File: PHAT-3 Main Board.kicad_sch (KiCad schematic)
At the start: 17 parts, among them K1 G5LE-1, P1 Power Terminal Block, P2 Power Terminal Block, P3 Power Terminal Block, P4 Power Terminal Block, U1 AHT21, U10 Logic Level Converter, U2 ESP32-S3 Dual-core SX1262, U3 BME280, U4 GY-521 MPU-6050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

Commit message: First Wiring Draft
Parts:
- removed K1: G5LE-1, Relay_THT:Relay_SPDT_Omron-G5LE-1, symbol Relay:G5LE-1
- added Q1: IRLZ44N, Package_TO_SOT_THT:TO-220-3_Vertical, symbol Transistor_FET:IRLZ44N
- added R3: 10k, Resistor_THT:R_Axial_DIN0207_L6.3mm_D2.5mm_P10.16mm_Horizontal, symbol Device:R
- R1, R2: value R -> 10k
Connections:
- net GND: now also P2.1 (GND), P4.1 (GND), U9.6 (GND), Q1.3 (S), R3.1; no longer U7.1 (GND)
- net at U6.2 (TXD): now also U2.10 (U2RXD); no longer U2.36 (U1RTS)
- net at U6.3 (RXD): now also U2.9 (U2TXD); no longer U2.35 (U1CTS)
- net +5V: now reaches U1.1 (VIN), U10.10 (HV), U2.20 (5V), U3.1 (VIN), U4.1 (VCC), U5.2 (OUT+), U6.5 (VCC), U7.2 (VDD), U8.1 (5V)
- net +5V: now also P2.2 (PWR), P4.2 (PWR), R1.1, R2.2, U9.5 (VCC)
- net at R2.1: now also U1.3 (SCL), U10.11 (HV2), U3.3 (SCL), U4.3 (SCL), U7.3 (SCL)
- net at U1.4 (SDA), U3.4 (SDA), U4.4 (SDA)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: now also R1.2, U10.12 (HV1); no longer U10.11 (HV2)
- net at U9.1 (CS): now also U2.29 (CS)
- net at U9.2 (SCK): now also U2.30 (SCK)
- net at U9.3 (MOSI): now also U2.31 (MOSI)
- net at U9.4 (MISO): now also U2.32 (MISO), R3.2
- net +15V: now reaches P1.2 (PWR), U5.1 (IN+)
- net +15V: now also P3.2 (PWR)
- net at U2.11 (U1TXD): now also U8.3 (RX)
- net at U2.12 (U1RXD): now also U8.2 (TX)
- net at U2.13 (SCL): now also U10.2 (LV2)
- net at U2.14 (SDA): now also U10.1 (LV1)
- net at U2.16 (3V3): now also U10.3 (LV)
- net at U2.22 (Ve): no longer U10.3 (LV)
- net at U2.23 (U0RXD): no longer U8.2 (TX)
- net at U2.24 (U0TXD): no longer U8.3 (RX)
- net at U2.27 (DATA): no longer U10.2 (LV2)
- net at U2.28 (HTR): now also Q1.1 (G); no longer U10.1 (LV1)
- net at P3.1 (GND): now also Q1.2 (D)
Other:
- note added: "Heater switch"
- note added: "Thumbcam power terminals"
- moved on the sheet: P1, P2, P3, P4, R1, R2, U1, U10, U2, U3, U4, U5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

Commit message: Finished Wiring and Implemented MOSFET
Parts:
- added R4: 100, Resistor_THT:R_Axial_DIN0207_L6.3mm_D2.5mm_P10.16mm_Horizontal, symbol Device:R
- added R5: 10k, Resistor_THT:R_Axial_DIN0207_L6.3mm_D2.5mm_P10.16mm_Horizontal, symbol Device:R
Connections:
- net GND: now also U2.18 (GND), U7.1 (GND), R5.1
- net at Q1.1 (G): now also R4.2, R5.2; no longer U2.28 (HTR)
- new net: R4.1, U2.28 (HTR)
- no-connect marks 0 -> 31
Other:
- moved on the sheet: P3, Q1, R3, U2, U9

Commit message: Rewired Everything Again
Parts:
- removed U3: BME280, Actual Footprint Library:BME280, symbol Footprint Library:BME280
- added C1: 100uF, Capacitor_THT:C_Radial_D5.0mm_H11.0mm_P2.00mm, symbol Device:C
- added C2, C3: 100nF, Capacitor_THT:C_Disc_D3.0mm_W2.0mm_P2.50mm, symbol Device:C
- added R6, R7: 10k, Resistor_THT:R_Axial_DIN0207_L6.3mm_D2.5mm_P10.16mm_Horizontal, symbol Device:R
- added U3: GY-68 BMP180, Actual Footprint Library:GY-68 BMP180, symbol Footprint Library:GY-68 BMP180
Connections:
- net +5V: now also C1.1, C2.2; no longer U1.1 (VIN), U7.2 (VDD)
- net GND: now also C1.2, C2.1, C3.2, U3.2 (GND)
- net at U2.13 (SCL): now also U1.3 (SCL), U10.1 (LV1), U7.3 (SCL), R7.2, U3.3 (SCL); no longer U10.2 (LV2)
- net at U2.14 (SDA): now also U1.4 (SDA), U10.2 (LV2), U7.4 (SDA), R6.2, U3.4 (SDA); no longer U10.1 (LV1)
- net at U2.16 (3V3): no longer U10.3 (LV)
- net +3V3: now reaches U2.17 (3V3)
- net +3V3: now also U1.1 (VIN), U10.3 (LV), U7.2 (VDD), C3.1, R6.1, R7.1, U3.1 (VIN)
- new net: R2.1, U10.11 (HV2), U4.4 (SDA)
- new net: R1.2, U10.12 (HV1), U4.3 (SCL)
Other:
- note added: "Buck converter"
- moved on the sheet: P1, P2, P3, P4, Q1, R1, R2, R3, R4, R5, U10, U2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

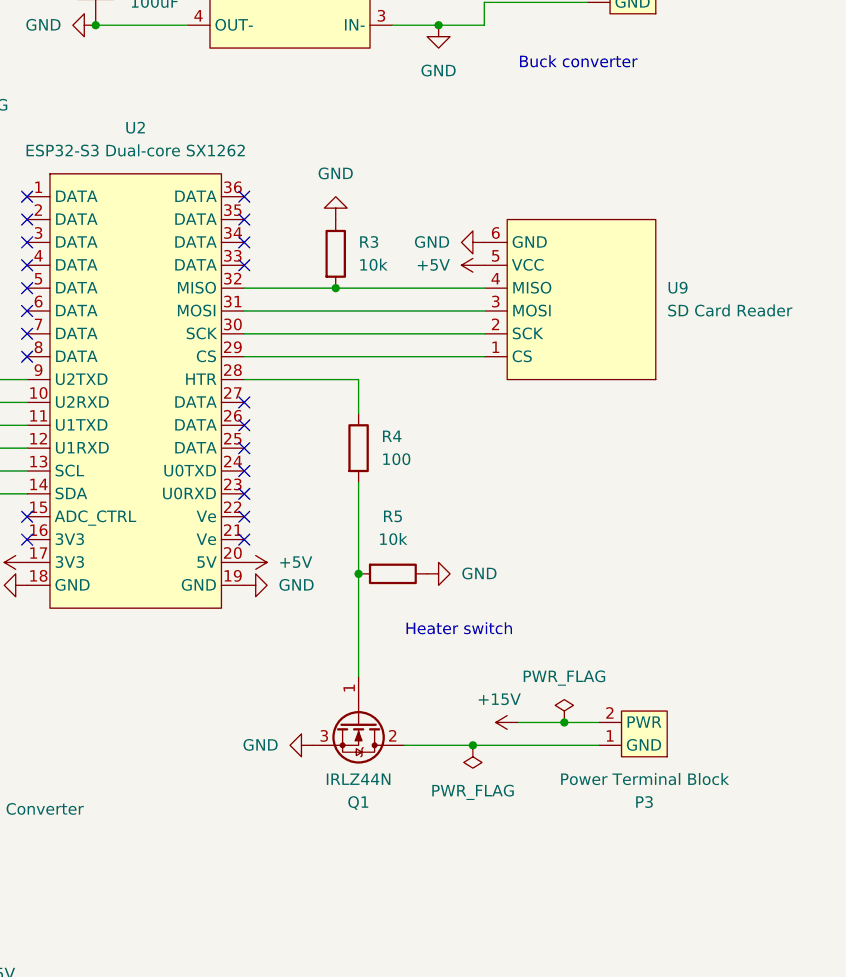
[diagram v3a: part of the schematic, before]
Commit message: Updated Footprint Sizes and SD Card Reader
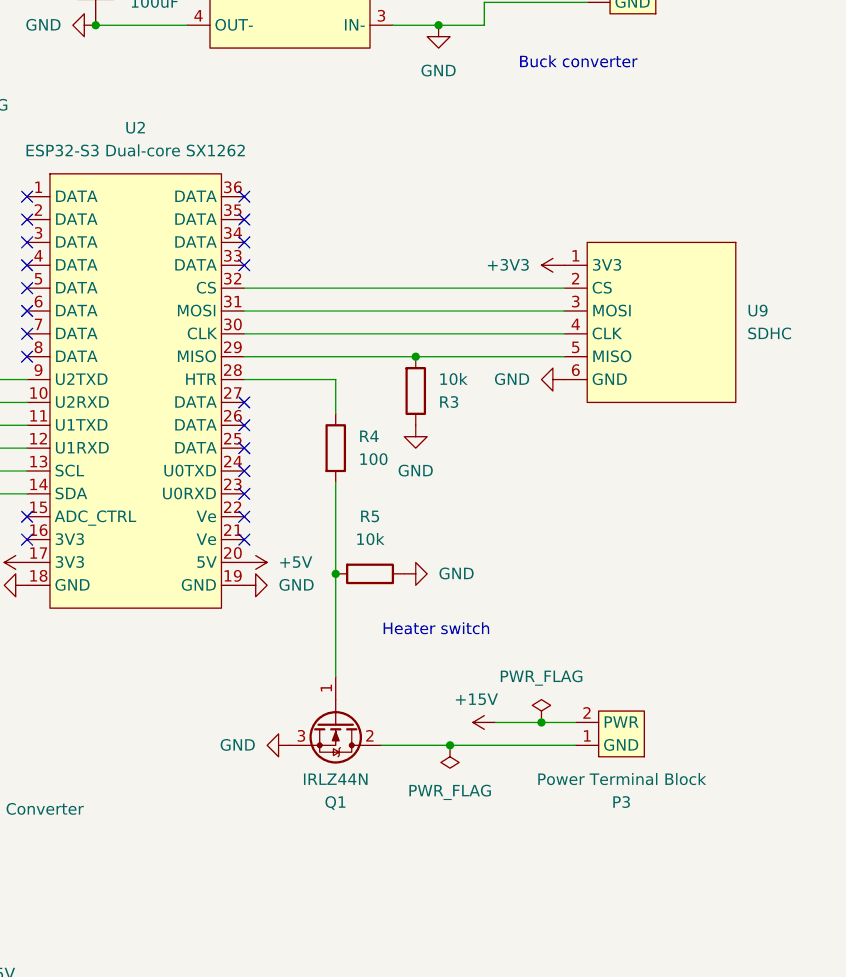
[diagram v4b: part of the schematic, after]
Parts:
- removed U9: SD Card Reader, Actual Footprint Library:SD Card Reader, symbol Footprint Library:SD_Card_Reader
- added U9: SDHC, Actual Footprint Library:SDHC, symbol Footprint Library:SDHC
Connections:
- net +3V3: now also U9.1 (3V3)
- net GND: now also U9.6 (GND)
- net at U2.29 (MISO): now also R3.2, U9.5 (MISO)
- net at U2.30 (CLK): now also U9.4 (CLK)
- net at U2.31 (MOSI): now also U9.3 (MOSI)
- net at U2.32 (CS): now also U9.2 (CS); no longer R3.2
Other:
- moved on the sheet: P3, Q1, R3, R4, R5

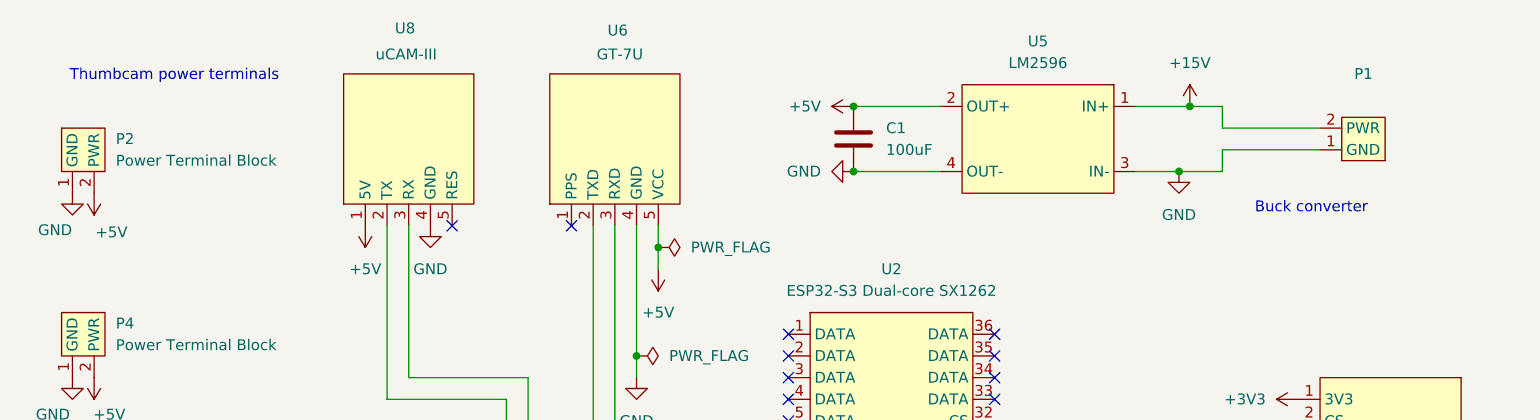
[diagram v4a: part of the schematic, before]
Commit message: Made a Preliminary PCB Layout
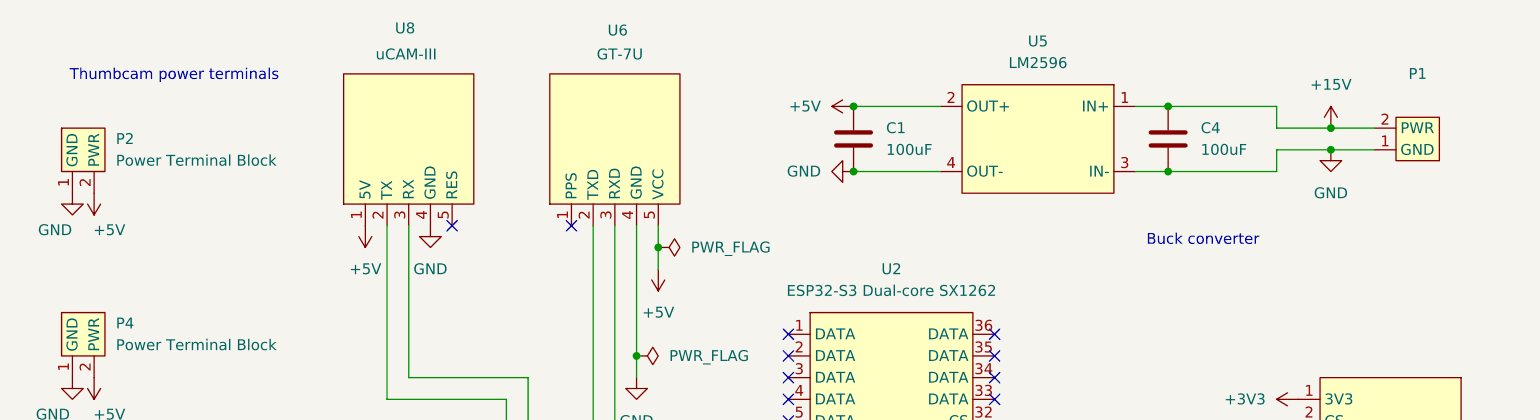
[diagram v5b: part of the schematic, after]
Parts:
- added C4: 100uF, Capacitor_THT:C_Radial_D5.0mm_H11.0mm_P2.00mm, symbol Device:C
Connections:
- net +15V: now also C4.1
- net GND: now also C4.2
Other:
- moved on the sheet: P1
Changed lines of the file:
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@@
 	)
 	(junction
+		(at 215.9 41.91)
+		(diameter 0)
+		(color 0 0 0 0)
+	)
+	(junction
 		(at 186.69 107.95)
 		(diameter 0)
@@
 	)
 	(junction
-		(at 199.39 39.37)
+		(at 95.25 121.92)
 		(diameter 0)
 		(color 0 0 0 0)
 	)
 	(junction
-		(at 95.25 121.92)
+		(at 196.85 46.99)
 		(diameter 0)
 		(color 0 0 0 0)
@@
 	)
 	(junction
+		(at 215.9 44.45)
+		(diameter 0)
+		(color 0 0 0 0)
+	)
+	(junction
 		(at 133.35 99.06)
 		(diameter 0)
@@
 	)
 	(junction
-		(at 198.12 46.99)
+		(at 95.25 96.52)
 		(diameter 0)
 		(color 0 0 0 0)
 	)
 	(junction
-		(at 95.25 96.52)
+		(at 209.55 124.46)
 		(diameter 0)
 		(color 0 0 0 0)
 	)
 	(junction
-		(at 209.55 124.46)
+		(at 133.35 157.48)
 		(diameter 0)
 		(color 0 0 0 0)
 	)
 	(junction
-		(at 133.35 157.48)
+		(at 196.85 39.37)
 		(diameter 0)
 		(color 0 0 0 0)
@@
 	(wire
 		(pts
+			(xy 196.85 39.37) (xy 209.55 39.37)
+		)
+		(stroke
+			(width 0)
+			(type default)
+		)
+	)
+	(wire
+		(pts
 			(xy 119.38 111.76) (xy 128.27 111.76)
 		)
@@
 	(wire
 		(pts
+			(xy 215.9 41.91) (xy 209.55 41.91)
+		)
+		(stroke
+			(width 0)
+			(type default)
+		)
+	)
+	(wire
+		(pts
 			(xy 95.25 121.92) (xy 95.25 149.86)
 		)
@@
 	(wire
 		(pts
-			(xy 203.2 44.45) (xy 203.2 46.99)
+			(xy 209.55 44.45) (xy 209.55 46.99)
 		)
 		(stroke
@@
 	(wire
 		(pts
-			(xy 203.2 46.99) (xy 198.12 46.99)
+			(xy 193.04 46.99) (xy 196.85 46.99)
 		)
 		(stroke
@@
 	(wire
 		(pts
+			(xy 215.9 44.45) (xy 209.55 44.45)
+		)
+		(stroke
+			(width 0)
+			(type default)
+		)
+	)
+	(wire
+		(pts
 			(xy 160.02 46.99) (xy 170.18 46.99)
 		)
@@
 	(wire
 		(pts
-			(xy 203.2 39.37) (xy 199.39 39.37)
+			(xy 193.04 39.37) (xy 196.85 39.37)
 		)
 		(stroke
@@
 	(wire
 		(pts
-			(xy 203.2 41.91) (xy 203.2 39.37)
+			(xy 209.55 41.91) (xy 209.55 39.37)
 		)
 		(stroke
@@
 	(wire
 		(pts
-			(xy 214.63 44.45) (xy 203.2 44.45)
+			(xy 220.98 44.45) (xy 215.9 44.45)
 		)
 		(stroke
@@
 	(wire
 		(pts
-			(xy 198.12 46.99) (xy 193.04 46.99)
+			(xy 92.71 119.38) (xy 92.71 147.32)
 		)
 		(stroke
@@
 	(wire
 		(pts
-			(xy 92.71 119.38) (xy 92.71 147.32)
+			(xy 160.02 39.37) (xy 170.18 39.37)
 		)
 		(stroke
@@
 	(wire
 		(pts
-			(xy 160.02 39.37) (xy 170.18 39.37)
+			(xy 121.92 71.12) (xy 121.92 91.44)
 		)
 		(stroke
@@
 	(wire
 		(pts
-			(xy 121.92 71.12) (xy 121.92 91.44)
+			(xy 119.38 148.59) (xy 130.81 148.59)
 		)
 		(stroke
@@
 	(wire
 		(pts
-			(xy 119.38 148.59) (xy 130.81 148.59)
+			(xy 135.89 138.43) (xy 135.89 152.4)
 		)
 		(stroke
@@
 	(wire
 		(pts
-			(xy 135.89 138.43) (xy 135.89 152.4)
+			(xy 196.85 46.99) (xy 209.55 46.99)
 		)
 		(stroke
@@
 	(wire
 		(pts
-			(xy 214.63 41.91) (xy 203.2 41.91)
+			(xy 220.98 41.91) (xy 215.9 41.91)
 		)
 		(stroke
@@
 	(wire
 		(pts
-			(xy 199.39 39.37) (xy 193.04 39.37)
-		)
-		(stroke
-			(width 0)
-			(type default)
-		)
-	)
-	(wire
-		(pts
 			(xy 186.69 107.95) (xy 186.69 119.38)
 		)
@@
 	(text "Buck converter"
 		(exclude_from_sim no)
-		(at 213.614 51.308 0)
+		(at 200.914 55.118 0)
 		(effects
 			(font
@@
 	(symbol
 		(lib_id "Device:C")
+		(at 196.85 43.18 0)
+		(unit 1)
+		(exclude_from_sim no)
+		(in_bom yes)
+		(on_board yes)
+		(dnp no)
+		(fields_autoplaced yes)
+		(property "Reference" "C4"
+			(at 200.66 41.9099 0)
+			(effects
+				(font
+					(size 1.27 1.27)
+				)
+				(justify left)
+			)
+		)
+		(property "Value" "100uF"
+			(at 200.66 44.4499 0)
+			(effects
+				(font
+					(size 1.27 1.27)
+				)
+				(justify left)
+			)
+		)
+		(property "Footprint" "Capacitor_THT:C_Radial_D5.0mm_H11.0mm_P2.00mm"
+			(at 197.8152 46.99 0)
+			(effects
+				(font
+					(size 1.27 1.27)
+				)
+				(hide yes)
+			)
+		)
+		(property "Datasheet" "~"
+			(at 196.85 43.18 0)
+			(effects
+				(font
+					(size 1.27 1.27)
+				)
+				(hide yes)
+			)
+		)
+		(property "Description" "Unpolarized capacitor"
+			(at 196.85 43.18 0)
+			(effects
+				(font
+					(size 1.27 1.27)
+				)
+				(hide yes)
+			)
+		)
+		(pin "2"
+		)
+		(pin "1"
+		)
+		(instances
+			(project "PHAT-3 Main Board"
+				(path "/da389c8a-9ca2-41c4-a7eb-3ce46ba4333b"
+					(reference "C4")
+					(unit 1)
+				)
+			)
+		)
+	)
+	(symbol
+		(lib_id "Device:C")
 		(at 160.02 43.18 0)
 		(unit 1)
@@
 		)
 		(property "Value" "+5V"
-			(at 73.152 54.102 0)
+			(at 72.898 53.848 0)
 			(effects
 				(font
@@
 	(symbol
 		(lib_id "Footprint Library:Power_Terminal_Block")
-		(at 217.17 44.45 270)
+		(at 223.52 44.45 270)
 		(mirror x)
 		(unit 1)
@@
 		(dnp no)
 		(property "Reference" "P1"
-			(at 219.71 35.56 90)
+			(at 226.06 35.56 90)
 			(effects
 				(font
@@
 		)
 		(property "Value" "Power Terminal Block"
-			(at 219.71 38.1 90)
+			(at 226.06 38.1 90)
 			(effects
 				(font
@@
 		)
 		(property "Footprint" "TerminalBlock_Phoenix:TerminalBlock_Phoenix_MKDS-1,5-2-5.08_1x02_P5.08mm_Horizontal"
-			(at 224.282 44.45 0)
+			(at 230.632 44.45 0)
 			(effects
 				(font
@@
 		)
 		(property "Datasheet" ""
-			(at 217.17 44.45 0)
+			(at 223.52 44.45 0)
 			(effects
 				(font
@@
 		)
 		(property "Description" ""
-			(at 217.17 44.45 0)
+			(at 223.52 44.45 0)
 			(effects
 				(font
@@
 	(symbol
 		(lib_id "power:+15V")
-		(at 199.39 39.37 0)
+		(at 215.9 41.91 0)
 		(unit 1)
 		(exclude_from_sim no)
@@
 		(fields_autoplaced yes)
 		(property "Reference" "#PWR030"
-			(at 199.39 43.18 0)
+			(at 215.9 45.72 0)
 			(effects
 				(font
@@
 		)
 		(property "Value" "+15V"
-			(at 199.39 34.29 0)
+			(at 215.9 36.83 0)
 			(effects
 				(font
@@
 		)
 		(property "Footprint" ""
-			(at 199.39 39.37 0)
+			(at 215.9 41.91 0)
 			(effects
 				(font
@@
 		)
 		(property "Datasheet" ""
-			(at 199.39 39.37 0)
+			(at 215.9 41.91 0)
 			(effects
 				(font
@@
 		)
 		(property "Description" "Power symbol creates a global label with name \"+15V\""
-			(at 199.39 39.37 0)
+			(at 215.9 41.91 0)
 			(effects
 				(font
@@
 	(symbol
 		(lib_id "power:GND")
-		(at 198.12 46.99 0)
+		(at 215.9 44.45 0)
 		(unit 1)
 		(exclude_from_sim no)
@@
 		(fields_autoplaced yes)
 		(property "Reference" "#PWR031"
-			(at 198.12 53.34 0)
+			(at 215.9 50.8 0)
 			(effects
 				(font
@@
 		)
 		(property "Value" "GND"
-			(at 198.12 52.07 0)
+			(at 215.9 49.53 0)
 			(effects
 				(font
@@
 		)
 		(property "Footprint" ""
-			(at 198.12 46.99 0)
+			(at 215.9 44.45 0)
 			(effects
 				(font
@@
 		)
 		(property "Datasheet" ""
-			(at 198.12 46.99 0)
+			(at 215.9 44.45 0)
 			(effects
 				(font
@@
 		)
 		(property "Description" "Power symbol creates a global label with name \"GND\" , ground"
-			(at 198.12 46.99 0)
+			(at 215.9 44.45 0)
 			(effects
 				(font

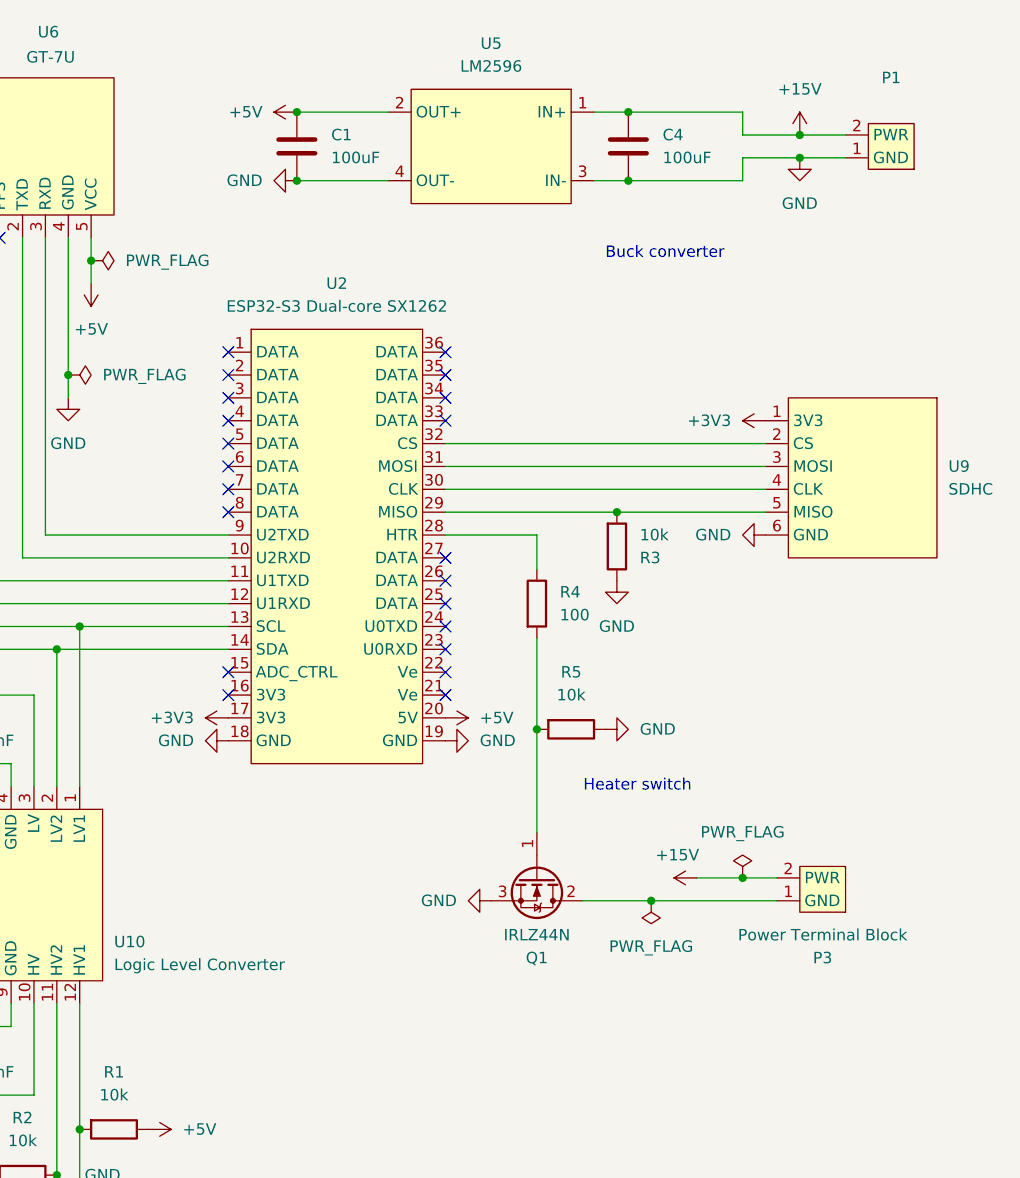
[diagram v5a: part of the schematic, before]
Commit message: Added Diodes and Switch
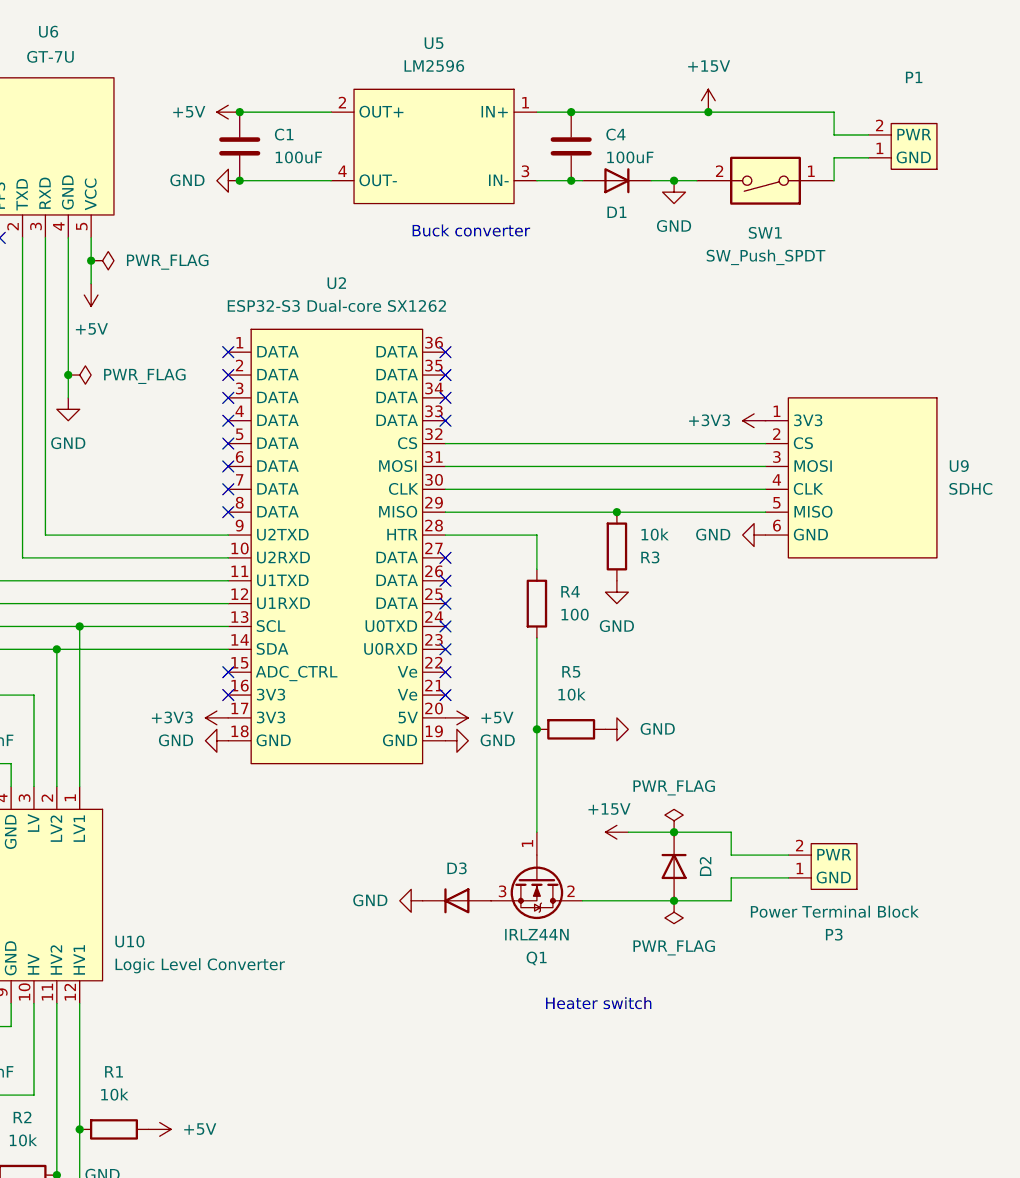
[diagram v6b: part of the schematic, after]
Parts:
- added D1, D2, D3: ~, Diode_THT:D_DO-27_P12.70mm_Horizontal, symbol Device:D
- added SW1: SW_Push_SPDT, Button_Switch_THT:SW_DIP_SPSTx01_Slide_9.78x4.72mm_W7.62mm_P2.54mm, symbol Switch:SW_DIP_x01
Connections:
- net +15V: now also D2.1 (K)
- net GND: now also D1.1 (K), D3.1 (K), SW1.2; no longer C4.2, P1.1 (GND), Q1.3 (S), U5.3 (IN-)
- net at P3.1 (GND), Q1.2 (D): now also D2.2 (A)
- new net: D3.2 (A), Q1.3 (S)
- new net: C4.2, D1.2 (A), U5.3 (IN-)
- new net: P1.1 (GND), SW1.1
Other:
- moved on the sheet: C1, C4, P1, P3, U5
